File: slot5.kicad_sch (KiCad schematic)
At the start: 1 part

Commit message: board layout
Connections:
- net AD1: now also PL6.a3 (Pin_a3); no longer PL6.b3 (Pin_b3)
- net Chroma: now also PL6.a2 (Pin_a2); no longer PL6.b2 (Pin_b2)
- net GND: now also PL6.b3 (Pin_b3); no longer PL6.a3 (Pin_a3)
- net Luma: now also PL6.b2 (Pin_b2); no longer PL6.a2 (Pin_a2)
- net VCLK: now reaches PL6.a38 (Pin_a38)
- net ESND: now reaches PL6.b10 (Pin_b10)
- no-connect marks 1 -> 0

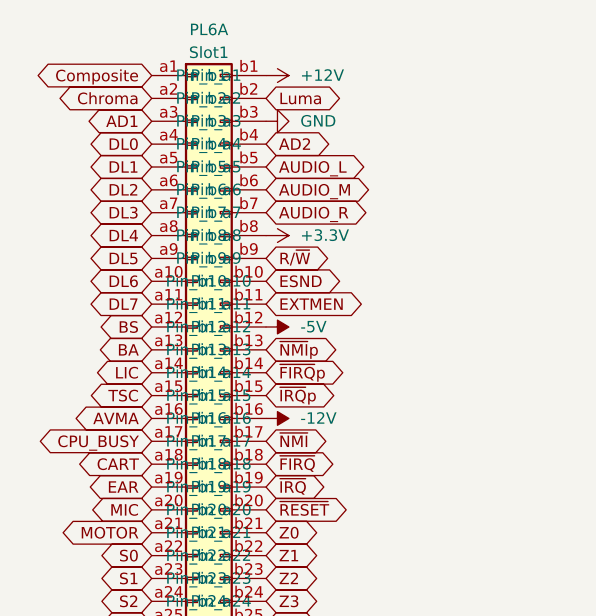
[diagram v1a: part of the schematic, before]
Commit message: revise bus tracing
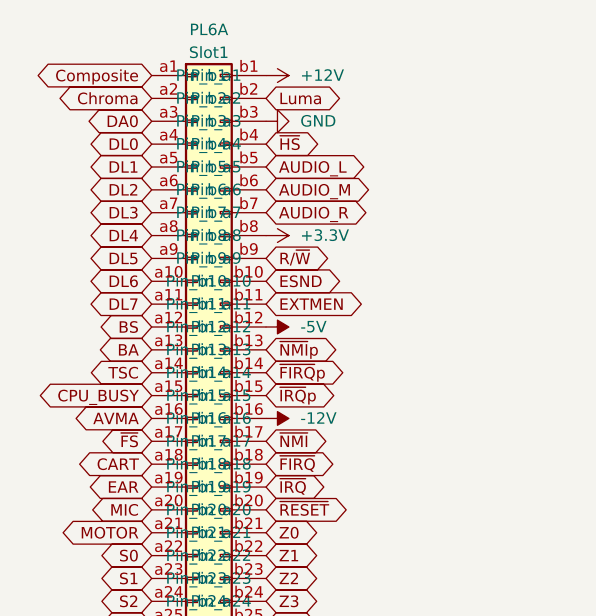
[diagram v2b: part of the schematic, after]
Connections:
- net LIC is gone; now on net TSC: PL6.a14 (Pin_a14)
- net CPU_BUSY: now also PL6.a15 (Pin_a15); no longer PL6.a17 (Pin_a17)
- net TSC: no longer PL6.a15 (Pin_a15)
- net AD1 renamed DA0
- net AD2 renamed ~{HS}
- new net ~{FS}: PL6.a17 (Pin_a17)
